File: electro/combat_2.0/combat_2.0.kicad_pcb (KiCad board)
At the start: 2 copper layers, 65.8 x 50 mm, 36 parts, among them J1 Screw_Terminal_01x02, J2 Screw_Terminal_01x02, J3 Screw_Terminal_01x02, J4 Screw_Terminal_01x02, J5 Conn_01x03_Pin, Q1 AO4402G, Q2 AO4402G, Q3 AO4402G, Q4 AO4402G, U1 ESP32-DevKitC, U2 AZ1117CH-5.0TRG1, U3 TB6612FNG, U4 LM2902, U5 ACS712xLCTR-20A

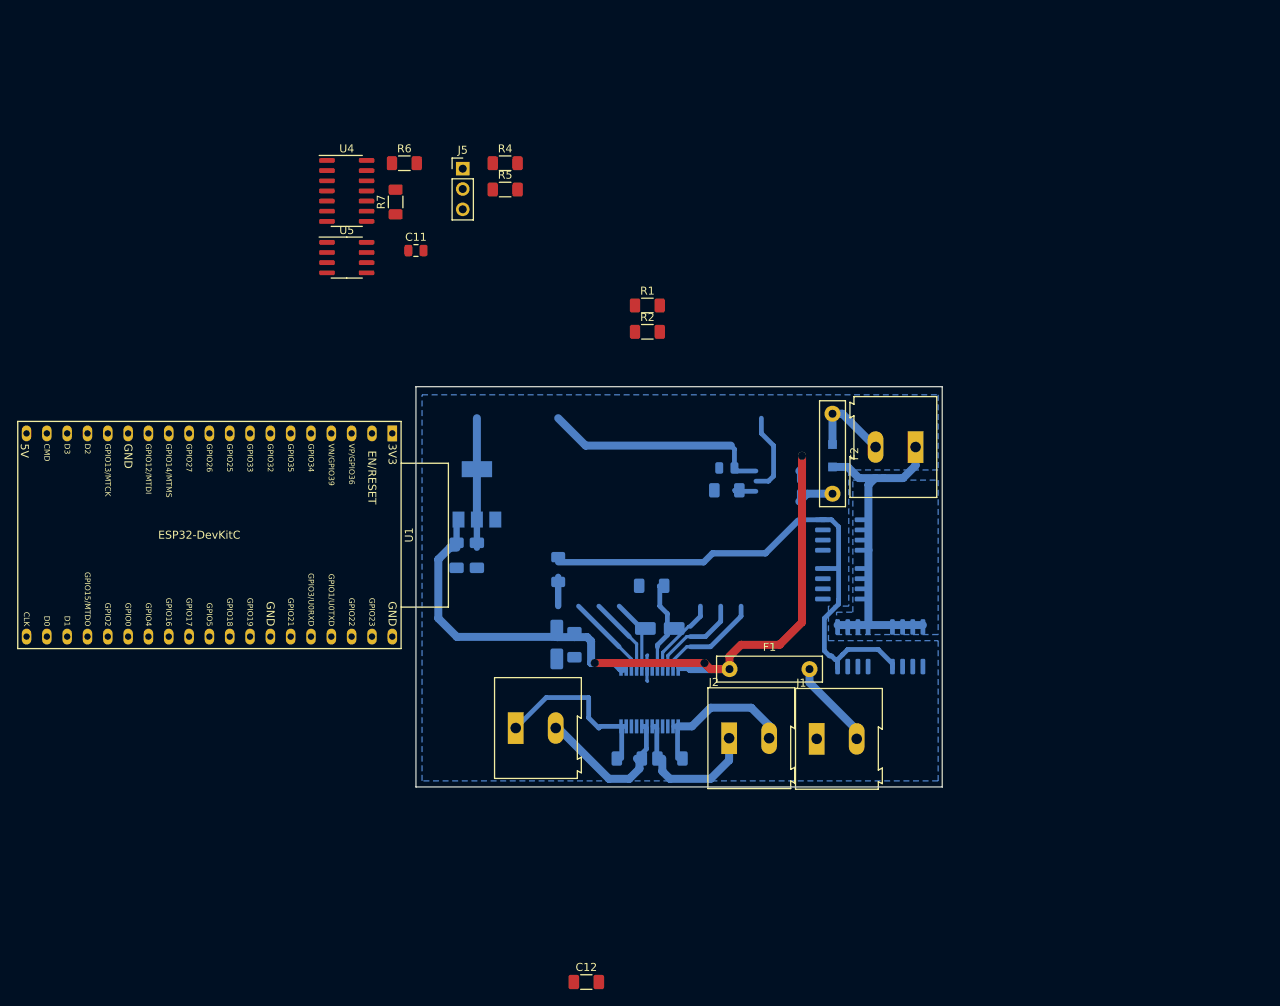
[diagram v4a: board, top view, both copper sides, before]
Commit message: Changed Devkit for ESP32-WROOM device. Added LDO, some other peripherals
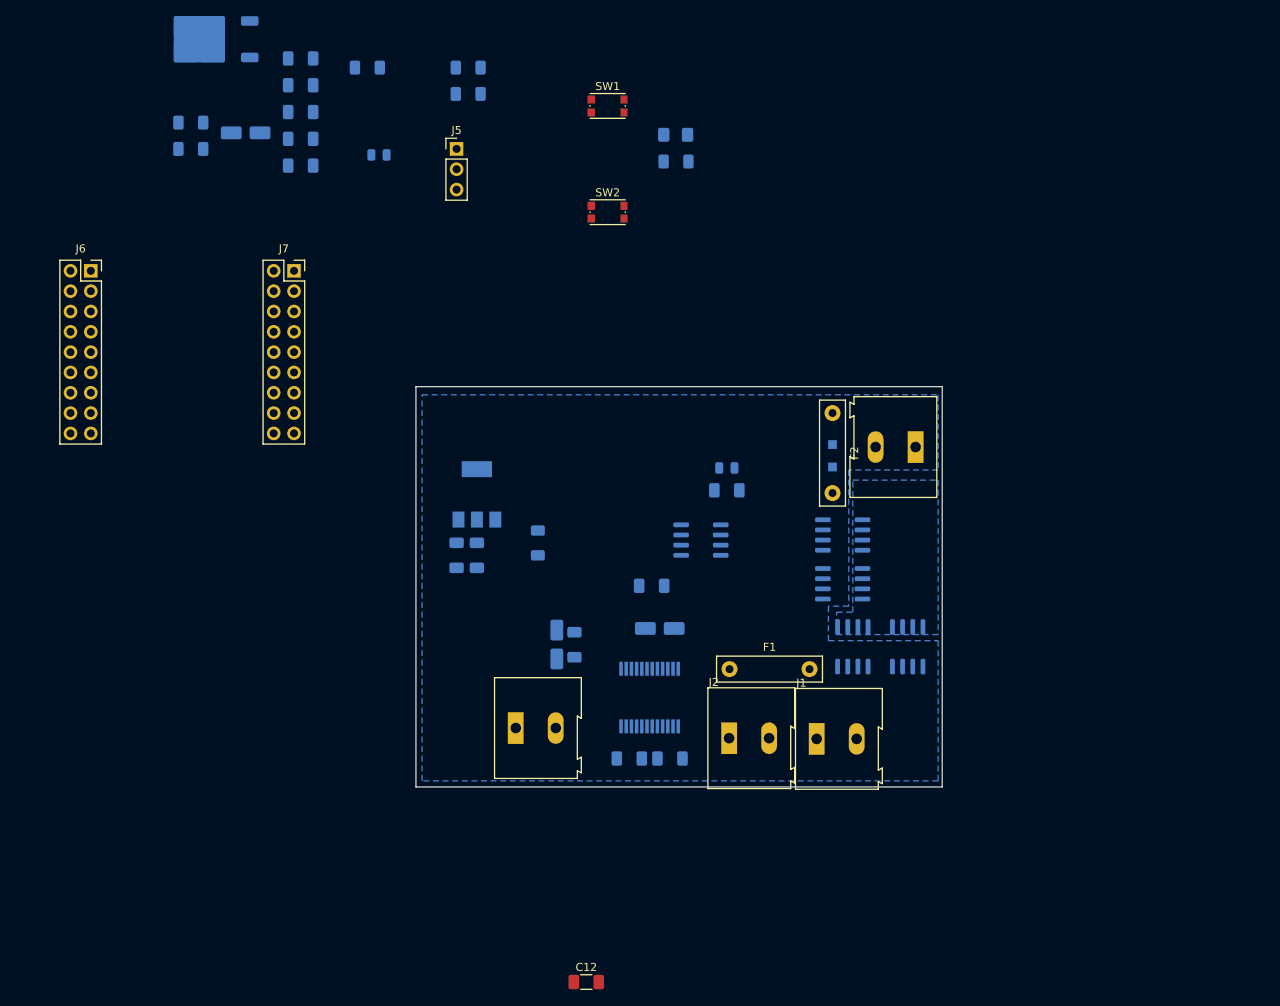
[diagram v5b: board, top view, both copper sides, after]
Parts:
- removed R1, R2: 10k, Resistor_SMD:R_1206_3216Metric_Pad1.30x1.75mm_HandSolder
- removed R3: R, Resistor_SMD:R_1206_3216Metric_Pad1.30x1.75mm_HandSolder
- removed U1: ESP32-DevKitC, Espressif:ESP32-DevKitC
- removed U4: LM2902, Package_SO:SOIC-14_3.9x8.7mm_P1.27mm
- added C13: 0.33uF, Capacitor_SMD:C_1206_3216Metric_Pad1.33x1.80mm_HandSolder, B.Cu at (46.5, 37.0)
- added C14: 10uF, Capacitor_SMD:CP_Elec_4x5.4, B.Cu at (39.7, 46.2)
- added C15: 0.1uF, Capacitor_SMD:C_1206_3216Metric_Pad1.33x1.80mm_HandSolder, B.Cu at (46.5, 40.3)
- added C16: 0.1uF, Capacitor_SMD:C_1206_3216Metric_Pad1.33x1.80mm_HandSolder, B.Cu at (46.5, 43.6)
- added C17: 22uF, Capacitor_SMD:C_1206_3216Metric_Pad1.33x1.80mm_HandSolder, B.Cu at (46.5, 47.0)
- added C18: 0.1uF, Capacitor_SMD:C_1206_3216Metric_Pad1.33x1.80mm_HandSolder, B.Cu at (46.5, 50.4)
- added D2: PWR, LED_SMD:LED_1206_3216Metric_Pad1.42x1.75mm_HandSolder, B.Cu at (93.4, 46.5)
- added J6: Conn_02x09_Odd_Even, Connector_PinSocket_2.54mm:PinSocket_2x09_P2.54mm_Vertical, F.Cu at (20.3, 63.5)
- added J7: Conn_02x09_Odd_Even, Connector_PinSocket_2.54mm:PinSocket_2x09_P2.54mm_Vertical, F.Cu at (45.7, 63.5)
- added R10: R, Resistor_SMD:R_1206_3216Metric_Pad1.30x1.75mm_HandSolder, B.Cu at (93.5, 49.8)
- added R8: 10kR, Resistor_SMD:R_1206_3216Metric_Pad1.30x1.75mm_HandSolder, B.Cu at (32.8, 45.0)
- added R9: 10kR, Resistor_SMD:R_1206_3216Metric_Pad1.30x1.75mm_HandSolder, B.Cu at (32.8, 48.3)
- added SW1: BOOT, Button_Switch_SMD:SW_Push_1P1T_NO_CK_KMR2, F.Cu at (84.9, 42.9)
- added SW2: EN, Button_Switch_SMD:SW_Push_1P1T_NO_CK_KMR2, F.Cu at (84.9, 56.2)
- added U6: LD29150DT33R, Package_TO_SOT_SMD:TO-252-2, B.Cu at (35.1, 34.5)
- C11, R4, R5, R6, R7, U5: moved to B.Cu
- J1: value Screw_Terminal_01x02 -> BATT
- J2: value Screw_Terminal_01x02 -> MOT_A
- J3: value Screw_Terminal_01x02 -> MOT_B
- J4: value Screw_Terminal_01x02 -> MOT_WPN
- J5: value Conn_01x03_Pin -> UART
- moved U5 56.6 mm to (96.6, 97.2), turned to 180 degrees
- moved R7 46.2 mm to (76.2, 97.5)
- moved R5 12.8 mm to (67.5, 41.4), turned to 180 degrees
- moved C11 12.8 mm to (56.3, 49.0), turned to 180 degrees
- moved R4 12.8 mm to (67.5, 38.1), turned to 180 degrees
- moved R6 12.8 mm to (54.9, 38.1), turned to 180 degrees
- moved J5 2.59 mm to (66.0, 48.3)
- moved F2 0.08 mm to (113.0, 81.3)
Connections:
- C6 pad 1: Net-(J2-Pin_2) -> Net-(J2-Pin_1)
- C6 pad 2: Net-(J2-Pin_1) -> Net-(J2-Pin_2)
- Q1 pad 4: /weapon_motor/PWM -> /PWM_WEAPON
- Q2 pad 4: /weapon_motor/PWM -> /PWM_WEAPON
- Q3 pad 4: /weapon_motor/PWM -> /PWM_WEAPON
- Q4 pad 4: /weapon_motor/PWM -> /PWM_WEAPON
- U3 pad 1: Net-(J2-Pin_2) -> Net-(J2-Pin_1)
- U3 pad 2: Net-(J2-Pin_2) -> Net-(J2-Pin_1)
- U3 pad 5: Net-(J2-Pin_1) -> Net-(J2-Pin_2)
- U3 pad 6: Net-(J2-Pin_1) -> Net-(J2-Pin_2)
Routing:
- net +8V: track 102.0 -> 0.00 mm, vias 3 -> 0
- net /weapon_motor/PWM: track 68.5 -> 0.00 mm
- net +5V: track 45.0 -> 0.00 mm
- net /weapon_motor/MOSFETS_DRAIN: track 43.3 -> 0.00 mm
- net Net-(J3-Pin_1): track 22.5 -> 0.00 mm
- net Net-(J3-Pin_2): track 19.9 -> 0.00 mm
- net Net-(J2-Pin_2): track 19.5 -> 0.00 mm
- net Net-(J2-Pin_1): track 18.7 -> 0.00 mm
- net /PWM_CH_A: track 13.1 -> 0.00 mm
- net /DIR_A_2: track 11.9 -> 0.00 mm
- net +3V3: track 11.3 -> 0.00 mm
- net Net-(J1-Pin_2): track 11.2 -> 0.00 mm
- net /weapon_motor/MOTOR_PWR: track 11.0 -> 0.00 mm
- net /PWM_CH_B: track 10.6 -> 0.00 mm
- net /MOTOR_CURRENT_ADC: track 10.3 -> 0.00 mm
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
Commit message: change connectors
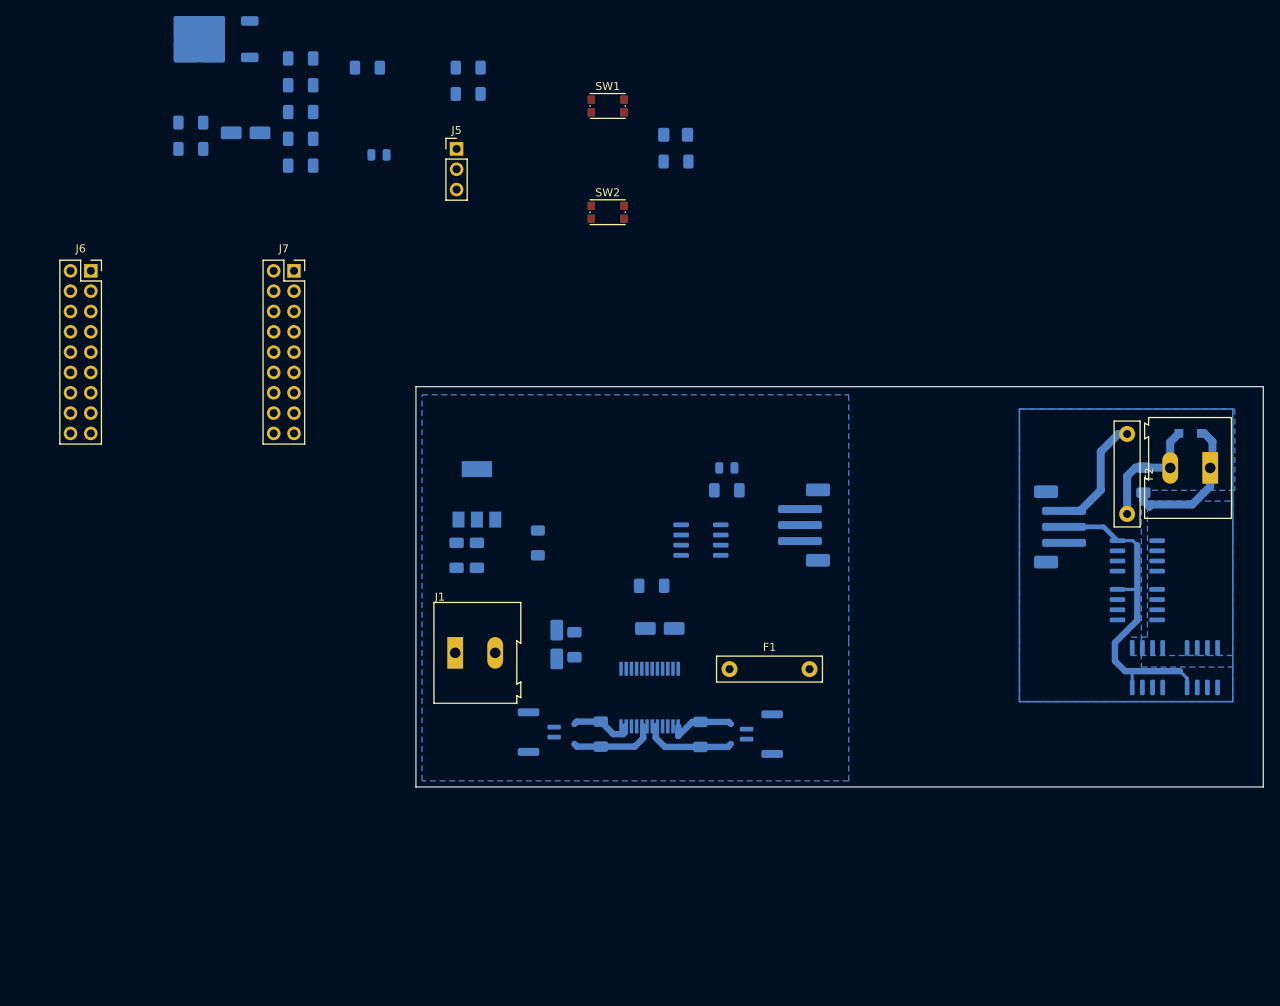
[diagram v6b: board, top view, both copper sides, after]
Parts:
- added J10: Conn_01x03_Pin, Connector_JST:JST_GH_SM02B-GHS-TB_1x02-1MP_P1.25mm_Horizontal, B.Cu at (104.1, 121.4)
- added J11: Conn_01x03_Pin, Connector_JST:JST_GH_SM02B-GHS-TB_1x02-1MP_P1.25mm_Horizontal, B.Cu at (76.4, 121.2)
- C12: moved to B.Cu
- J2: value MOT_A -> Conn_01x04_Pin; footprint TerminalBlock:TerminalBlock_Altech_AK300-2_P5.00mm -> Connector_JST:JST_PH_B3B-PH-SM4-TB_1x03-1MP_P2.00mm_Vertical; moved to B.Cu
- J3: value MOT_B -> Conn_01x04_Pin; footprint TerminalBlock:TerminalBlock_Altech_AK300-2_P5.00mm -> Connector_JST:JST_PH_B3B-PH-SM4-TB_1x03-1MP_P2.00mm_Vertical; moved to B.Cu
- moved C12 93.7 mm to (151.9, 89.7), turned to -90 degrees
- moved J3 72.5 mm to (141.5, 95.5), turned to -90 degrees
- moved J1 46.5 mm to (65.9, 111.3)
- moved D1 44.8 mm to (157.7, 83.8), turned to 0 degrees
- moved F2 36.9 mm to (149.9, 83.9)
- moved Q1 36.9 mm to (159.3, 113.1)
- moved Q2 36.9 mm to (152.4, 113.1)
- moved J4 36.9 mm to (160.2, 88.1)
- moved Q3 36.9 mm to (151.1, 105.2)
- moved Q4 36.9 mm to (151.1, 99.1)
- moved J2 28.2 mm to (109.5, 95.3), turned to 90 degrees
- moved C6 4.86 mm to (96.5, 121.5), turned to -90 degrees
- moved C7 4.68 mm to (84.1, 121.4), turned to -90 degrees
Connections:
- C12 pad 1: /weapon_motor/MOTOR_PWR -> /weapon_motor/MOTOR_IN
- C6 pad 1: Net-(J2-Pin_1) -> Net-(J10-Pin_1)
- C6 pad 2: Net-(J2-Pin_2) -> Net-(J10-Pin_2)
- C7 pad 1: Net-(J3-Pin_1) -> Net-(J11-Pin_2)
- C7 pad 2: Net-(J3-Pin_2) -> Net-(J11-Pin_1)
- D1 pad 1: /weapon_motor/MOTOR_PWR -> /weapon_motor/MOTOR_IN
- F2 pad 2: Net-(F2-Pad2) -> /weapon_motor/MOTOR_IN
- J2 pad 1: Net-(J2-Pin_1) -> GND
- J2 pad 2: Net-(J2-Pin_2) -> /PWM_WEAPON
- J3 pad 1: Net-(J3-Pin_1) -> /weapon_motor/MOTOR_PWR
- J3 pad 2: Net-(J3-Pin_2) -> /PWM_WEAPON
- J4 pad 2: /weapon_motor/MOTOR_PWR -> /weapon_motor/MOTOR_IN
- U3 pad 1: Net-(J2-Pin_1) -> Net-(J10-Pin_1)
- U3 pad 11: Net-(J3-Pin_1) -> Net-(J11-Pin_2)
- U3 pad 12: Net-(J3-Pin_1) -> Net-(J11-Pin_2)
- U3 pad 2: Net-(J2-Pin_1) -> Net-(J10-Pin_1)
- U3 pad 5: Net-(J2-Pin_2) -> Net-(J10-Pin_2)
- U3 pad 6: Net-(J2-Pin_2) -> Net-(J10-Pin_2)
- U3 pad 7: Net-(J3-Pin_2) -> Net-(J11-Pin_1)
- U3 pad 8: Net-(J3-Pin_2) -> Net-(J11-Pin_1)
- U5 pad 3: Net-(F2-Pad2) -> /weapon_motor/MOTOR_PWR
- U5 pad 4: Net-(F2-Pad2) -> /weapon_motor/MOTOR_PWR
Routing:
- net /PWM_WEAPON: track 0.00 -> 41.4 mm
- net /weapon_motor/MOSFETS_DRAIN: track 0.00 -> 18.2 mm
- net /weapon_motor/MOTOR_IN: track 0.00 -> 15.3 mm
- net /weapon_motor/MOTOR_PWR: track 0.00 -> 14.7 mm
- net Net-(J10-Pin_2): track 0.00 -> 11.5 mm
- net Net-(J11-Pin_1): track 0.00 -> 10.6 mm
- net Net-(J10-Pin_1): track 0.00 -> 8.63 mm
- net Net-(J11-Pin_2): track 0.00 -> 7.92 mm
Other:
- board size 65.8 x 50 mm -> 105.9 x 50 mm

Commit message: almost ready pcb
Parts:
- removed C10: 0.1uF, Capacitor_SMD:C_0805_2012Metric
- removed C14: 10uF, Capacitor_SMD:CP_Elec_4x5.4
- removed C5, C6: 0.1uF, Capacitor_SMD:C_1206_3216Metric_Pad1.33x1.80mm_HandSolder
- removed D2: PWR, LED_SMD:LED_1206_3216Metric_Pad1.42x1.75mm_HandSolder
- removed R10: R, Resistor_SMD:R_1206_3216Metric_Pad1.30x1.75mm_HandSolder
- removed R9: 10kR, Resistor_SMD:R_1206_3216Metric_Pad1.30x1.75mm_HandSolder
- removed U5: ACS712xLCTR-20A, Package_SO:SOIC-8_3.9x4.9mm_P1.27mm
- removed U6: LD29150DT33R, Package_TO_SOT_SMD:TO-252-2
- added D3: D, Diode_SMD:D_SOD-123F, B.Cu at (153.2, 89.7)
- added J12: MOT_WPN, TerminalBlock:TerminalBlock_Altech_AK300-2_P5.00mm, F.Cu at (160.5, 87.1)
- added J13: Conn_02x09_Odd_Even, Connector_PinSocket_2.54mm:PinSocket_2x09_P2.54mm_Vertical, F.Cu at (105.9, 85.6)
- added J14: Conn_02x09_Odd_Even, Connector_PinSocket_2.54mm:PinSocket_2x09_P2.54mm_Vertical, F.Cu at (78.0, 85.6)
- added J8: Conn_01x01_Pin, TestPoint:TestPoint_Keystone_5019_Minature, B.Cu at (140.5, 105.7)
- added J9: Conn_01x01_Pin, TestPoint:TestPoint_Keystone_5019_Minature, B.Cu at (62.0, 103.4)
- added R1: R, Resistor_SMD:R_1206_3216Metric_Pad1.30x1.75mm_HandSolder, B.Cu at (92.7, 83.3)
- added R2: 220, Resistor_SMD:R_1206_3216Metric_Pad1.30x1.75mm_HandSolder, B.Cu at (68.6, 84.6)
- added R3: 10kR, Resistor_SMD:R_1206_3216Metric_Pad1.30x1.75mm_HandSolder, B.Cu at (91.9, 89.7)
- added U1: AZ1117CH-5.0TRG1, Package_TO_SOT_SMD:SOT-223-3_TabPin2, B.Cu at (110.3, 114.2)
- added U4: ACS712xLCTR-20A, Package_SO:SOIC-8_3.9x4.9mm_P1.27mm, B.Cu at (69.1, 104.9)
- C1: value 10uF -> 0.1uF
- C11: value ~ -> 22uF; footprint Capacitor_SMD:C_0805_2012Metric -> Capacitor_SMD:C_0805_2012Metric_Pad1.18x1.45mm_HandSolder
- C12, C16, C18, C2, C7: footprint Capacitor_SMD:C_1206_3216Metric_Pad1.33x1.80mm_HandSolder -> Capacitor_SMD:C_0805_2012Metric_Pad1.18x1.45mm_HandSolder
- C13: value 0.33uF -> 0.1uF; footprint Capacitor_SMD:C_1206_3216Metric_Pad1.33x1.80mm_HandSolder -> Capacitor_SMD:C_0805_2012Metric_Pad1.18x1.45mm_HandSolder
- C15: value 0.1uF -> 1nF; footprint Capacitor_SMD:C_1206_3216Metric_Pad1.33x1.80mm_HandSolder -> Capacitor_SMD:C_0805_2012Metric_Pad1.18x1.45mm_HandSolder
- C17: value 22uF -> 1uF; footprint Capacitor_SMD:C_1206_3216Metric_Pad1.33x1.80mm_HandSolder -> Capacitor_SMD:C_0805_2012Metric_Pad1.18x1.45mm_HandSolder
- C3: value 0.1uF -> 22uF
- C4: value 10uF -> 22uF; footprint Capacitor_SMD:CP_Elec_4x5.4 -> Capacitor_SMD:C_0805_2012Metric_Pad1.18x1.45mm_HandSolder
- C8: value 10uF -> 1uF; footprint Capacitor_SMD:CP_Elec_4x5.4 -> Capacitor_SMD:C_0805_2012Metric_Pad1.18x1.45mm_HandSolder
- C9: value 1nF -> 22uF; footprint Capacitor_SMD:C_1206_3216Metric_Pad1.33x1.80mm_HandSolder -> Capacitor_SMD:C_0805_2012Metric_Pad1.18x1.45mm_HandSolder
- D1: value D -> PWR; footprint Diode_SMD:D_SOD-123F -> LED_SMD:LED_PLCC-2_3x2mm_AK
- J10, J11: value Conn_01x03_Pin -> Conn_01x01_Pin; footprint Connector_JST:JST_GH_SM02B-GHS-TB_1x02-1MP_P1.25mm_Horizontal -> TestPoint:TestPoint_Keystone_5019_Minature
- J2: value Conn_01x04_Pin -> Conn_01x02_Socket; footprint Connector_JST:JST_PH_B3B-PH-SM4-TB_1x03-1MP_P2.00mm_Vertical -> Connector_PinHeader_2.54mm:PinHeader_1x02_P2.54mm_Vertical
- J3: value Conn_01x04_Pin -> UART; footprint Connector_JST:JST_PH_B3B-PH-SM4-TB_1x03-1MP_P2.00mm_Vertical -> Connector_PinHeader_2.54mm:PinHeader_1x03_P2.54mm_Vertical; moved to F.Cu
- J4: value MOT_WPN -> Conn_01x03_Pin; footprint TerminalBlock:TerminalBlock_Altech_AK300-2_P5.00mm -> Connector_Molex:Molex_PicoBlade_53398-0271_1x02-1MP_P1.25mm_Vertical; moved to B.Cu
- J5: value UART -> Conn_01x03_Pin; footprint Connector_PinHeader_2.54mm:PinHeader_1x03_P2.54mm_Vertical -> Connector_Molex:Molex_PicoBlade_53398-0271_1x02-1MP_P1.25mm_Vertical; moved to B.Cu
- J6, J7: value Conn_02x09_Odd_Even -> Conn_01x01_Pin; footprint Connector_PinSocket_2.54mm:PinSocket_2x09_P2.54mm_Vertical -> TestPoint:TestPoint_Keystone_5019_Minature; moved to B.Cu
- R4: footprint Resistor_SMD:R_1206_3216Metric_Pad1.30x1.75mm_HandSolder -> Resistor_THT:R_Axial_DIN0204_L3.6mm_D1.6mm_P7.62mm_Horizontal
- R6: value 2k7R -> 220; footprint Resistor_SMD:R_1206_3216Metric_Pad1.30x1.75mm_HandSolder -> Resistor_THT:R_Axial_DIN0204_L3.6mm_D1.6mm_P7.62mm_Horizontal
- R7: value 4k7R -> 2k7R
- R8: value 10kR -> 4k7R
- SW1: value BOOT -> EN
- SW2: value EN -> BOOT
- U2: value AZ1117CH-5.0TRG1 -> LD29150DT33R; footprint Package_TO_SOT_SMD:SOT-223-3_TabPin2 -> Package_TO_SOT_SMD:SOT-353_SC-70-5
- moved J6 123.5 mm to (141.2, 88.9), turned to 180 degrees
- moved C18 118.1 mm to (157.2, 91.7), turned to -90 degrees
- moved J7 100.6 mm to (140.5, 97.3), turned to 180 degrees
- moved C13 90.6 mm to (84.1, 119.3), turned to -90 degrees
- moved J4 85.4 mm to (80.4, 118.3), turned to 90 degrees
- moved J5 78.1 mm to (100.0, 118.6), turned to -90 degrees
- moved R5 77.3 mm to (48.7, 116.3)
- moved R6 73.0 mm to (92.2, 100.8), turned to 0 degrees
- moved D1 70.6 mm to (87.1, 83.8), turned to 180 degrees
- moved R4 69.7 mm to (52.6, 106.2)
- moved C11 67.5 mm to (83.8, 110.7), turned to -90 degrees
- moved C12 63.2 mm to (96.0, 119.1)
- moved C15 62.7 mm to (67.1, 99.6)
- moved R8 60.4 mm to (65.8, 95.5), turned to -90 degrees
- moved C16 59.9 mm to (71.1, 98.3), turned to 90 degrees
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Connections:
- C1 pad 1: +8V -> GND
- C1 pad 2: GND -> /ESP32 PCB adapter/EN
- C11 pad 1: /MOTOR_CURRENT_ADC -> +8V
- C12 pad 1: /weapon_motor/MOTOR_IN -> Net-(J5-Pin_1)
- C12 pad 2: /weapon_motor/MOSFETS_DRAIN -> Net-(J5-Pin_2)
- C13 pad 1: +8V -> Net-(J4-Pin_2)
- C13 pad 2: GND -> Net-(J4-Pin_1)
- C15 pad 1: /ESP32 PCB adapter/IO0 -> Net-(U4-FILTER)
- C16 pad 1: GND -> +5V
- C16 pad 2: /ESP32 PCB adapter/EN -> GND
- C17 pad 1: +3V3 -> /MOTOR_CURRENT_ADC
- C18 pad 1: +3V3 -> /weapon_motor/MOTOR_IN
- C18 pad 2: GND -> /weapon_motor/MOSFETS_DRAIN
- C2 pad 1: +5V -> +8V
- C4 pad 1: +3V3 -> +5V
- C7 pad 1: Net-(J11-Pin_2) -> /ESP32 PCB adapter/IO0
- C7 pad 2: Net-(J11-Pin_1) -> GND
- C8 pad 1: +8V -> +3V3
- C9 pad 1: Net-(U5-FILTER) -> +3V3
- D1 pad 1: /weapon_motor/MOTOR_IN -> GND
- D1 pad 2: /weapon_motor/MOSFETS_DRAIN -> Net-(D1-A)
- J10 pad 1: Net-(J10-Pin_1) -> /PWM_WEAPON
- J11 pad 1: Net-(J11-Pin_1) -> /weapon_motor/MOTOR_PWR
- J2 pad 1: GND -> Net-(J2-Pin_1)
- J2 pad 2: /PWM_WEAPON -> /ESP32 PCB adapter/IO35
- J3 pad 1: /weapon_motor/MOTOR_PWR -> /UART_TX
- J3 pad 2: /PWM_WEAPON -> /UART_RX
- J4 pad 1: /weapon_motor/MOSFETS_DRAIN -> Net-(J4-Pin_1)
- J4 pad 2: /weapon_motor/MOTOR_IN -> Net-(J4-Pin_2)
- J5 pad 1: /UART_TX -> Net-(J5-Pin_1)
- J5 pad 2: /UART_RX -> Net-(J5-Pin_2)
- J6 pad 1: /ESP32 PCB adapter/SVP -> /weapon_motor/MOTOR_PWR
- J7 pad 1: +3V3 -> /PWM_WEAPON
- R6 pad 1: Net-(U5-VIOUT) -> +3V3
- R6 pad 2: /MOTOR_CURRENT_ADC -> /ESP32 PCB adapter/IO16
- R7 pad 1: /MOTOR_CURRENT_ADC -> Net-(U4-VIOUT)
- R7 pad 2: GND -> /MOTOR_CURRENT_ADC
- R8 pad 1: /ESP32 PCB adapter/IO16 -> /MOTOR_CURRENT_ADC
- R8 pad 2: +3V3 -> GND
- SW1 pad 1: /ESP32 PCB adapter/IO0 -> GND
- SW1 pad 2: GND -> /ESP32 PCB adapter/EN
- SW2 pad 1: GND -> /ESP32 PCB adapter/IO0
- SW2 pad 2: /ESP32 PCB adapter/EN -> GND
- U2 pad 1: GND -> +5V
- U2 pad 2: +5V -> GND
- U2 pad 3: +8V -> +5V
- U3 pad 1: Net-(J10-Pin_1) -> Net-(J5-Pin_1)
- U3 pad 11: Net-(J11-Pin_2) -> Net-(J4-Pin_2)
- U3 pad 12: Net-(J11-Pin_2) -> Net-(J4-Pin_2)
- U3 pad 2: Net-(J10-Pin_1) -> Net-(J5-Pin_1)
- U3 pad 5: Net-(J10-Pin_2) -> Net-(J5-Pin_2)
- U3 pad 6: Net-(J10-Pin_2) -> Net-(J5-Pin_2)
- U3 pad 7: Net-(J11-Pin_1) -> Net-(J4-Pin_1)
- U3 pad 8: Net-(J11-Pin_1) -> Net-(J4-Pin_1)
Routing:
- net +5V: track 0.00 -> 77.0 mm, vias 0 -> 2
- net +3V3: track 0.00 -> 74.0 mm
- net +8V: track 0.00 -> 71.3 mm, vias 0 -> 1
- net /DIR_A_1: track 0.00 -> 26.3 mm
- net /DIR_B_1: track 0.00 -> 24.0 mm
- net /DIR_A_2: track 0.00 -> 22.6 mm
- net /PWM_WEAPON: track 41.4 -> 63.8 mm
- net /DIR_B_2: track 0.00 -> 21.6 mm
- net /PWM_CH_A: track 0.00 -> 19.6 mm
- net /PWM_CH_B: track 0.00 -> 18.8 mm
- net GND: track 0.00 -> 12.2 mm, vias 0 -> 5
- net Net-(J10-Pin_2): track 11.5 -> 0.00 mm
- net Net-(J5-Pin_2): track 0.00 -> 10.9 mm
- net Net-(J11-Pin_1): track 10.6 -> 0.00 mm
- net /ESP32 PCB adapter/EN: track 0.00 -> 10.5 mm
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- added copper zone on F.Cu, net GND
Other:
- board size 105.9 x 50 mm -> 110.7 x 51.6 mm
